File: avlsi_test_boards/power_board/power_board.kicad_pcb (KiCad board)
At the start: 6 copper layers, 99.9 x 100 mm, 100 parts, among them J1 PJ-102AH, J2 PJ-102AH, U1 TLV1117LV18DCYR, U11 TLV75709PDBV, U12 SN74LVC16T245DLR, U13 SN74LVC16T245DLR, U14 SN74LVC16T245DLR, U15 SN74LVC16T245DLR, U16 SN74LVC16T245DLR, U17 SN74LVC16T245DLR, U2 TLV1117LV25DCYR, U3 TLV1117LV33DCYR, U4 DS04-254-2-04BK-SMT, U5 74HC4051D_653, U6 TLV1117LV18DCYR, U7 TLV75709PDBV, U8 TLV1117LV25DCYR, U9 TLV1117LV33DCYR

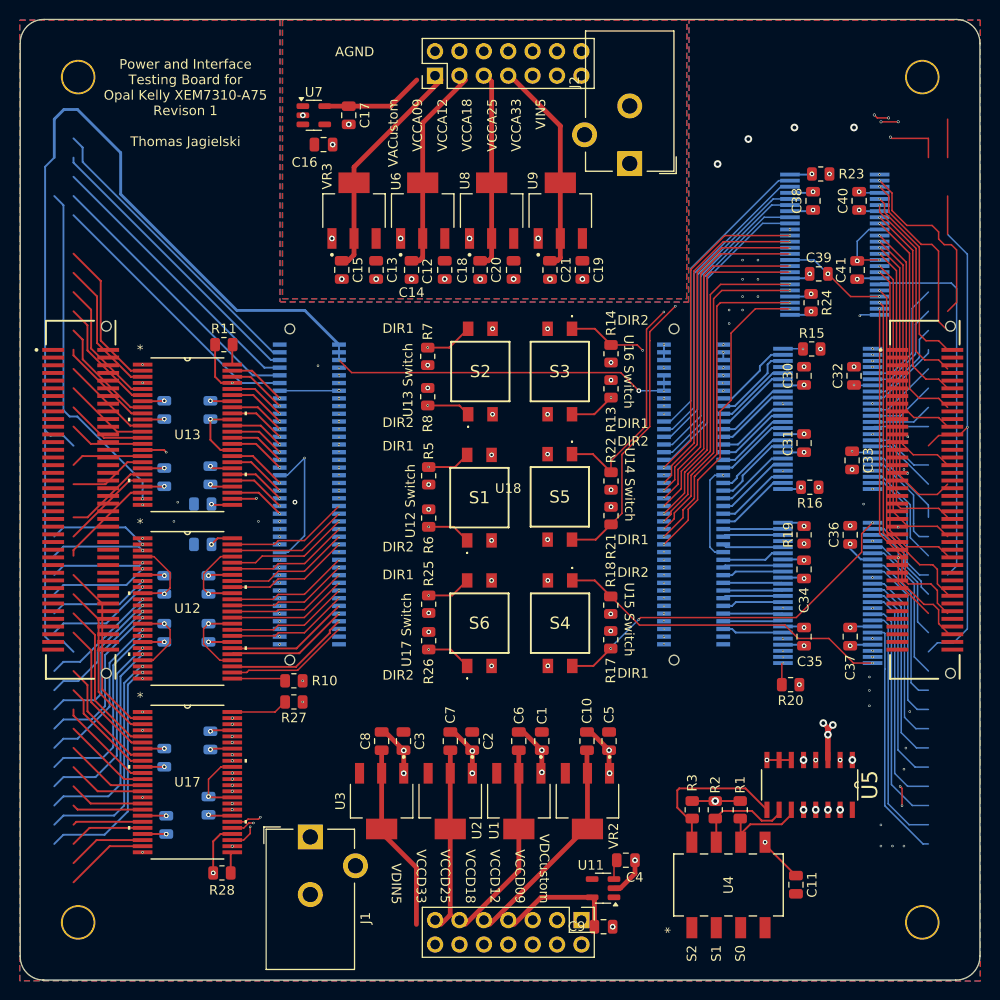
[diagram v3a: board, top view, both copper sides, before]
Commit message: Add updated power board layout and schematic
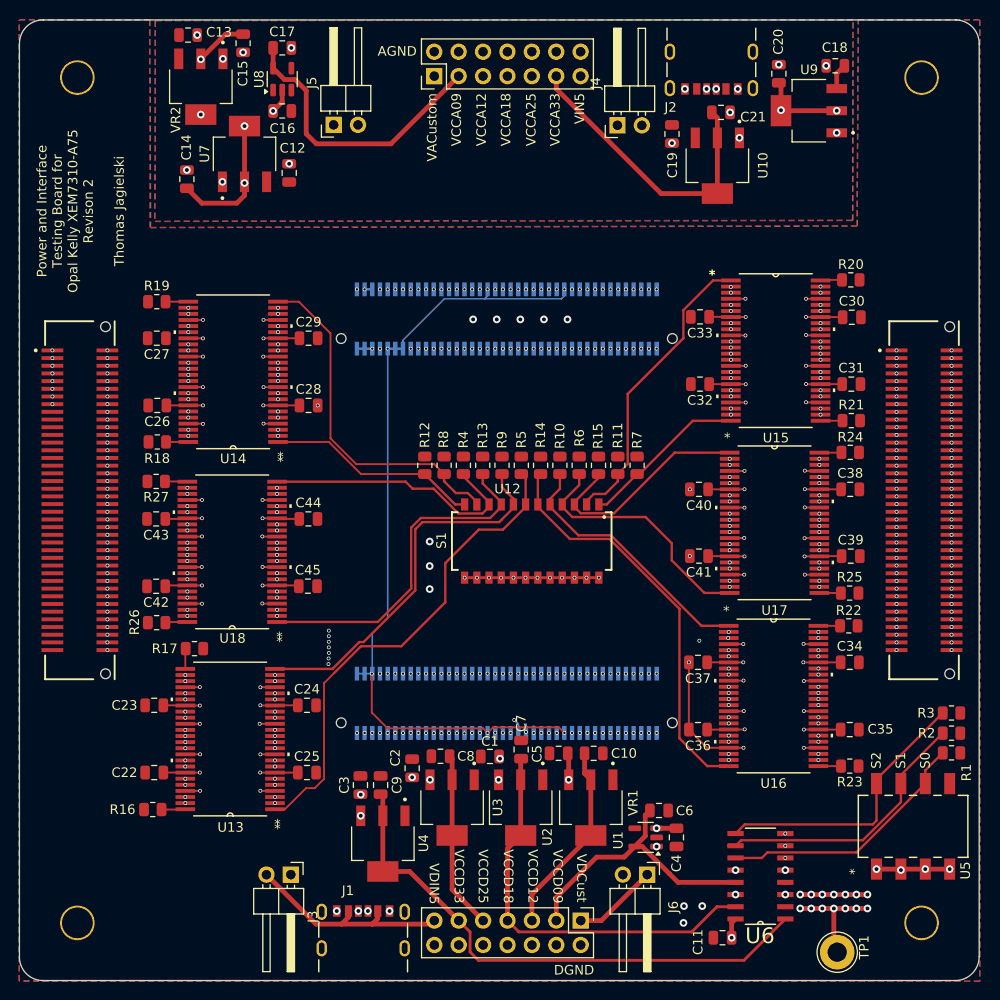
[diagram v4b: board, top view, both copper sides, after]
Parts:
- removed R28: 10k, Resistor_SMD:R_0805_2012Metric
- removed S2, S3, S4, S5, S6: 2454985-3, 2_DS:24549853
- removed VR3: TLV1117LV12DCYR, avlsi:VREG_TLV1117LV12DCYR
- added J3: Conn_01x02_Pin, Connector_PinHeader_2.54mm:PinHeader_1x02_P2.54mm_Horizontal, F.Cu at (128.4, 114.4)
- added J4: Conn_01x02_Pin, Connector_PinHeader_2.54mm:PinHeader_1x02_P2.54mm_Horizontal, F.Cu at (162.4, 36.4)
- added J5: Conn_01x02_Pin, Connector_PinHeader_2.54mm:PinHeader_1x02_P2.54mm_Horizontal, F.Cu at (132.8, 36.3)
- added J6: Conn_01x02_Pin, Connector_PinHeader_2.54mm:PinHeader_1x02_P2.54mm_Horizontal, F.Cu at (165.5, 114.4)
- added R4: 4.7k, Resistor_SMD:R_0805_2012Metric, F.Cu at (146.3, 71.8)
- added TP1: TestPoint, TestPoint:TestPoint_Loop_D3.80mm_Drill2.0mm, F.Cu at (185.2, 122.5)
- added VR1: TLV1117LV12DCYR, avlsi:VREG_TLV1117LV12DCYR, F.Cu at (159.6, 107.4)
- C22, C23, C24, C25, C26, C27, C28, C29, C42, C43, C44, C45, U14, U15, U16: moved to F.Cu
- J1, J2: value PJ-102AH -> 2171750001; footprint Connector_BarrelJack:BarrelJack_CUI_PJ-102AH_Horizontal -> avlsi_preferred_parts:MOLEX_2171750001
- R10, R11, R15: value 10k -> 4.7k
- R12, R9: value 10k -> 4.7k; moved to F.Cu
- R17, R18, R21, R22, R25, R26: value 4.7k -> 10k
- S1: value 2454985-3 -> 416131160812; footprint 2_DS:24549853 -> avlsi_preferred_parts:416131160812
- U1: value TLV1117LV18DCYR -> TLV75709PDBV; footprint avlsi:SOT230P700X180-4N -> Package_TO_SOT_SMD:SOT-23-5
- U10: value ~ -> TLV1117LV33DCYR; footprint avlsi:opal_kelly_XEM7310_header -> avlsi:VREG_TLV1117LV33DCYR; moved to F.Cu
- U11: value TLV75709PDBV -> ~; footprint Package_TO_SOT_SMD:SOT-23-5 -> avlsi:opal_kelly_XEM7310_header; moved to B.Cu
- U12: value SN74LVC16T245DLR -> ~; footprint avlsi:DL48 -> avlsi_preferred_parts:power_board
- U18: value ~ -> SN74LVC16T245DLR; footprint avlsi_preferred_parts:power_board -> avlsi:DL48
- U2: value TLV1117LV25DCYR -> TLV1117LV18DCYR
- U3, U9: value TLV1117LV33DCYR -> TLV1117LV25DCYR; footprint avlsi:VREG_TLV1117LV33DCYR -> avlsi:SOT230P700X180-4N
- U4: value DS04-254-2-04BK-SMT -> TLV1117LV33DCYR; footprint ds:DS04-254-2-04BK-SMT_CUD -> avlsi:VREG_TLV1117LV33DCYR
- U5: value 74HC4051D_653 -> DS04-254-2-04BK-SMT; footprint 74HC4051D_653:SOIC127P600X175-16N -> ds:DS04-254-2-04BK-SMT_CUD
- U6: value TLV1117LV18DCYR -> 74HC4051D_653; footprint avlsi:SOT230P700X180-4N -> 74HC4051D_653:SOIC127P600X175-16N
- U7: value TLV75709PDBV -> TLV1117LV18DCYR; footprint Package_TO_SOT_SMD:SOT-23-5 -> avlsi:SOT230P700X180-4N
- U8: value TLV1117LV25DCYR -> TLV75709PDBV; footprint avlsi:SOT230P700X180-4N -> Package_TO_SOT_SMD:SOT-23-5
- moved VR2 84.6 mm to (119.0, 32.4)
- moved U6 77.7 mm to (177.3, 114.5), turned to 180 degrees
- moved R16 76.2 mm to (114.0, 107.6), turned to 0 degrees
- moved R19 71.6 mm to (114.4, 54.7), turned to 0 degrees
- moved U17 66.8 mm to (178.7, 77.8)
- moved U14 62.1 mm to (122.4, 62.0)
- moved R23 61.7 mm to (186.6, 103.1)
- moved R18 50.2 mm to (114.5, 69.3), turned to 0 degrees
- moved U16 47.4 mm to (178.6, 95.8), turned to 0 degrees
- moved R25 43.8 mm to (186.5, 85.1), turned to 180 degrees
- moved R17 43.3 mm to (118.3, 90.8), turned to 180 degrees
- moved R11 42.9 mm to (162.4, 71.8), turned to -90 degrees
- moved R20 42.6 mm to (186.7, 52.5)
- moved U10 41.3 mm to (172.8, 40.6), turned to -90 degrees
- moved C25 40.6 mm to (130.1, 103.8), turned to 0 degrees
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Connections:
- C22 pad 1: VCCD33 -> V_Level_Shift
- C23 pad 1: VCCD33 -> V_Level_Shift
- C24 pad 1: V_Level_Shift -> VCCD33
- C25 pad 1: V_Level_Shift -> VCCD33
- C26 pad 1: VCCD33 -> V_Level_Shift
- C27 pad 1: VCCD33 -> V_Level_Shift
- C28 pad 1: V_Level_Shift -> VCCD33
- C29 pad 1: V_Level_Shift -> VCCD33
- C30 pad 1: VCCD33 -> V_Level_Shift
- C31 pad 1: VCCD33 -> V_Level_Shift
- C32 pad 1: V_Level_Shift -> VCCD33
- C33 pad 1: V_Level_Shift -> VCCD33
- C34 pad 1: VCCD33 -> V_Level_Shift
- C35 pad 1: VCCD33 -> V_Level_Shift
- C36 pad 1: V_Level_Shift -> VCCD33
- C37 pad 1: V_Level_Shift -> VCCD33
- C38 pad 1: VCCD33 -> V_Level_Shift
- C39 pad 1: VCCD33 -> V_Level_Shift
- C40 pad 1: V_Level_Shift -> VCCD33
- C41 pad 1: V_Level_Shift -> VCCD33
- C42 pad 1: VCCD33 -> V_Level_Shift
- C43 pad 1: VCCD33 -> V_Level_Shift
- C44 pad 1: V_Level_Shift -> VCCD33
- C45 pad 1: V_Level_Shift -> VCCD33
- C6 pad 1: VCCD18 -> VCCD09
- C7 pad 1: VCCD25 -> VCCD18
- C8 pad 1: VCCD33 -> VCCD25
- C9 pad 1: VCCD09 -> VCCD33
- R10 pad 2: Net-(U12-*2OE) -> /level_shifters/LS10_DIR1
- R11 pad 2: Net-(U13-*1OE) -> /level_shifters/LS9_DIR1
- R12 pad 2: Net-(U13-*2OE) -> /level_shifters/LS8_DIR1
- R13 pad 1: /level_shifter3/DIR1 -> DGND
- R13 pad 2: DGND -> /level_shifters/LS12_DIR1
- R14 pad 1: /level_shifter3/DIR2 -> DGND
- R14 pad 2: DGND -> /level_shifters/LS10_DIR2
- R15 pad 2: Net-(U14-*1OE) -> /level_shifters/LS11_DIR1
- R16 pad 2: Net-(U14-*2OE) -> Net-(U13-*1OE)
- R17 pad 1: /level_shifter4/DIR1 -> DGND
- R17 pad 2: DGND -> Net-(U13-*2OE)
- R18 pad 1: /level_shifter4/DIR2 -> DGND
- R18 pad 2: DGND -> Net-(U14-*1OE)
- R19 pad 2: Net-(U15-*1OE) -> Net-(U14-*2OE)
- R20 pad 2: Net-(U15-*2OE) -> Net-(U15-*1OE)
- R21 pad 1: /level_shifter5/DIR1 -> DGND
- R21 pad 2: DGND -> Net-(U15-*2OE)
- R22 pad 1: /level_shifter5/DIR2 -> DGND
- R22 pad 2: DGND -> Net-(U16-*1OE)
- R23 pad 2: Net-(U16-*1OE) -> Net-(U16-*2OE)
- R24 pad 2: Net-(U16-*2OE) -> Net-(U17-*1OE)
- R25 pad 1: /level_shifter6/DIR1 -> DGND
- R25 pad 2: DGND -> Net-(U17-*2OE)
- R26 pad 1: /level_shifter6/DIR2 -> DGND
- R26 pad 2: DGND -> Net-(U18-*1OE)
- R27 pad 2: Net-(U17-*1OE) -> Net-(U18-*2OE)
- R5 pad 1: /level_shifter1/DIR1 -> DGND
- R5 pad 2: DGND -> /level_shifters/LS7_DIR1
- R6 pad 1: /level_shifter1/DIR2 -> DGND
- R6 pad 2: DGND -> /level_shifters/LS11_DIR2
- R7 pad 1: /level_shifter2/DIR1 -> DGND
- R7 pad 2: DGND -> /level_shifters/LS9_DIR2
- R8 pad 1: /level_shifter2/DIR2 -> DGND
- R8 pad 2: DGND -> /level_shifters/LS8_DIR2
- R9 pad 2: Net-(U12-*1OE) -> /level_shifters/LS7_DIR2
- S1 pad A1: /level_shifter1/DIR2 -> VCCD33
- U1 pad 1: DGND -> DVIN5
- U1 pad 2: VCCD18 -> DGND
- U1 pad 4: VCCD18 -> unconnected-(U1-NC-Pad4)
- U12 pad 10: DGND -> MC1_19_PIN
- U12 pad 11: MC2_58_PIN -> MC1_26_PIN
- U12 pad 12: MC2_60_PIN -> MC1_21_PIN
- U12 pad 13: MC2_62_PIN -> MC1_28_PIN
- U12 pad 14: MC2_64_PIN -> MC1_23_PIN
- U12 pad 15: DGND -> MC1_30_PIN
- U12 pad 16: MC2_66_PIN -> MC1_25_PIN
- U12 pad 17: MC2_68_PIN -> unconnected-(U12A-MC1_17-Pad17)
- U12 pad 18: V_Level_Shift -> MC1_27_PIN
- U12 pad 19: MC2_70_PIN -> unconnected-(U12A-MC1_19-Pad19)
- U12 pad 20: MC2_72_PIN -> MC1_29_PIN
- U12 pad 21: DGND -> unconnected-(U12A-MC1_21-Pad21)
- U12 pad 22: MC2_74_PIN -> MC1_31_PIN
- U12 pad 23: MC2_76_PIN -> unconnected-(U12A-MC1_23-Pad23)
- U12 pad 24: /level_shifter1/DIR2 -> MC1_33_PIN
- U12 pad 25: Net-(U12-*2OE) -> unconnected-(U12A-MC1_25-Pad25)
- U12 pad 26: MC2_76 -> MC1_37_PIN
- U12 pad 27: MC2_74 -> unconnected-(U12A-MC1_27-Pad27)
- U12 pad 28: DGND -> MC1_39_PIN
- U12 pad 29: MC2_72 -> unconnected-(U12A-MC1_29-Pad29)
- U12 pad 30: MC2_70 -> MC1_41_PIN
- U12 pad 31: VCCD33 -> unconnected-(U12A-MC1_31-Pad31)
- U12 pad 32: MC2_68 -> MC1_43_PIN
- U12 pad 33: MC2_66 -> unconnected-(U12A-MC1_33-Pad33)
- U12 pad 34: DGND -> MC2_26_PIN
- U12 pad 35: MC2_64 -> unconnected-(U12A-DGND-Pad35)
- U12 pad 36: MC2_62 -> MC2_24_PIN
- U12 pad 37: MC2_60 -> unconnected-(U12A-MC1_37-Pad37)
- U12 pad 38: MC2_58 -> MC2_22_PIN
- U12 pad 39: DGND -> unconnected-(U12A-MC1_39-Pad39)
- U12 pad 40: MC2_54 -> MC2_20_PIN
- U12 pad 41: MC2_52 -> unconnected-(U12A-MC1_41-Pad41)
- U12 pad 42: VCCD33 -> MC2_18_PIN
- U12 pad 43: MC2_50 -> unconnected-(U12A-MC1_43-Pad43)
- U12 pad 44: MC2_48 -> MC2_16_PIN
- U12 pad 45: DGND -> unconnected-(U12A-MC1_45-Pad45)
- U12 pad 46: MC2_46 -> MC2_12_PIN
- U12 pad 47: MC2_44 -> unconnected-(U12A-MC1_47-Pad47)
- U12 pad 48: Net-(U12-*1OE) -> MC2_10_PIN
- U13 pad 1: /level_shifter2/DIR1 -> /level_shifters/LS7_DIR1
- U13 pad 11: MC2_27_PIN -> MC2_17
- U13 pad 12: MC2_29_PIN -> MC2_15
- U13 pad 13: MC2_31_PIN -> MC2_31
- U13 pad 14: MC2_33_PIN -> MC2_33
- U13 pad 16: MC2_37_PIN -> MC2_37
- U13 pad 17: MC2_39_PIN -> MC2_39
- U13 pad 18: V_Level_Shift -> VCCD33
- U13 pad 19: MC2_41_PIN -> MC2_41
- U13 pad 2: MC2_15_PIN -> MC2_29
- U13 pad 20: MC2_43_PIN -> MC2_43
- U13 pad 22: MC2_45_PIN -> MC2_45
- U13 pad 23: MC2_10_PIN -> MC2_47
- U13 pad 24: /level_shifter2/DIR2 -> /level_shifters/LS7_DIR2
- U13 pad 26: MC2_10 -> MC2_47_PIN
- U13 pad 27: MC2_45 -> MC2_45_PIN
- U13 pad 29: MC2_43 -> MC2_43_PIN
- U13 pad 3: MC2_17_PIN -> MC2_27
- U13 pad 30: MC2_41 -> MC2_41_PIN
- U13 pad 31: VCCD33 -> V_Level_Shift
- U13 pad 32: MC2_39 -> MC2_39_PIN
- U13 pad 33: MC2_37 -> MC2_37_PIN
- U13 pad 35: MC2_33 -> MC2_33_PIN
- U13 pad 36: MC2_31 -> MC2_31_PIN
- U13 pad 37: MC2_29 -> MC2_15_PIN
- U13 pad 38: MC2_27 -> MC2_17_PIN
- U13 pad 40: MC2_25 -> MC2_19_PIN
- U13 pad 41: MC2_23 -> MC2_21_PIN
- U13 pad 42: VCCD33 -> V_Level_Shift
- U13 pad 43: MC2_21 -> MC2_23_PIN
- U13 pad 44: MC2_19 -> MC2_25_PIN
- U13 pad 46: MC2_17 -> MC2_27_PIN
- U13 pad 47: MC2_15 -> MC2_29_PIN
- U13 pad 5: MC2_19_PIN -> MC2_25
- U13 pad 6: MC2_21_PIN -> MC2_23
- U13 pad 7: V_Level_Shift -> VCCD33
- U13 pad 8: MC2_23_PIN -> MC2_21
- U13 pad 9: MC2_25_PIN -> MC2_19
- U14 pad 1: /level_shifter3/DIR1 -> /level_shifters/LS8_DIR1
- U14 pad 11: MC1_28_PIN -> MC1_34
- U14 pad 12: MC1_30_PIN -> MC1_32
- U14 pad 13: MC1_32_PIN -> MC1_30
- U14 pad 14: MC1_34_PIN -> MC1_28
- U14 pad 16: MC1_38_PIN -> MC1_26
- U14 pad 17: MC1_40_PIN -> MC1_24
- U14 pad 18: V_Level_Shift -> VCCD33
- U14 pad 19: MC1_42_PIN -> MC1_22
- U14 pad 2: MC1_16_PIN -> MC1_25
- U14 pad 20: MC1_44_PIN -> MC1_20
- U14 pad 22: MC1_46_PIN -> MC1_18
- U14 pad 23: MC1_48_PIN -> MC1_16
- U14 pad 24: /level_shifter3/DIR2 -> /level_shifters/LS8_DIR2
- U14 pad 26: MC1_48 -> MC1_16_PIN
- U14 pad 27: MC1_46 -> MC1_18_PIN
- U14 pad 29: MC1_44 -> MC1_20_PIN
- U14 pad 3: MC1_18_PIN -> MC1_23
- U14 pad 30: MC1_42 -> MC1_22_PIN
- U14 pad 31: VCCD33 -> V_Level_Shift
- U14 pad 32: MC1_40 -> MC1_24_PIN
- U14 pad 33: MC1_38 -> MC1_26_PIN
- U14 pad 35: MC1_34 -> MC1_28_PIN
- U14 pad 36: MC1_32 -> MC1_30_PIN
- U14 pad 37: MC1_30 -> MC1_32_PIN
- U14 pad 38: MC1_28 -> MC1_34_PIN
- U14 pad 40: MC1_26 -> MC1_15_PIN
- U14 pad 41: MC1_24 -> MC1_17_PIN
- U14 pad 42: VCCD33 -> V_Level_Shift
- U14 pad 43: MC1_22 -> MC1_19_PIN
- U14 pad 44: MC1_20 -> MC1_21_PIN
- U14 pad 46: MC1_18 -> MC1_23_PIN
- U14 pad 47: MC1_16 -> MC1_25_PIN
- U14 pad 5: MC1_20_PIN -> MC1_21
- U14 pad 6: MC1_22_PIN -> MC1_19
- U14 pad 7: V_Level_Shift -> VCCD33
- U14 pad 8: MC1_24_PIN -> MC1_17
- U14 pad 9: MC1_26_PIN -> MC1_15
- U15 pad 1: /level_shifter4/DIR1 -> /level_shifters/LS9_DIR1
- U15 pad 11: MC1_64_PIN -> MC1_64
- U15 pad 12: MC1_66_PIN -> MC1_62
- U15 pad 13: MC1_68_PIN -> MC1_60
- U15 pad 14: MC1_70_PIN -> MC1_58
- U15 pad 16: MC1_72_PIN -> MC1_54
- U15 pad 17: MC1_74_PIN -> MC1_52
- U15 pad 18: V_Level_Shift -> VCCD33
- U15 pad 19: MC1_76_PIN -> MC1_50
- U15 pad 2: MC1_50_PIN -> MC1_74
- U15 pad 20: MC1_15_PIN -> MC1_79
- U15 pad 22: MC1_17_PIN -> MC1_77
- U15 pad 23: MC1_19_PIN -> MC1_75
- U15 pad 24: /level_shifter4/DIR2 -> /level_shifters/LS9_DIR2
- U15 pad 26: MC1_19 -> MC1_75_PIN
- U15 pad 27: MC1_17 -> MC1_77_PIN
- U15 pad 29: MC1_15 -> MC1_79_PIN
- U15 pad 3: MC1_52_PIN -> MC1_76
- U15 pad 30: MC1_76 -> MC1_50_PIN
- U15 pad 31: VCCD33 -> V_Level_Shift
- U15 pad 32: MC1_74 -> MC1_52_PIN
- U15 pad 33: MC1_72 -> MC1_54_PIN
- U15 pad 35: MC1_70 -> MC1_58_PIN
- U15 pad 36: MC1_68 -> MC1_60_PIN
- U15 pad 37: MC1_66 -> MC1_62_PIN
- U15 pad 38: MC1_64 -> MC1_64_PIN
- U15 pad 40: MC1_62 -> MC1_66_PIN
- U15 pad 41: MC1_60 -> MC1_68_PIN
- U15 pad 42: VCCD33 -> V_Level_Shift
- U15 pad 43: MC1_58 -> MC1_70_PIN
- U15 pad 44: MC1_54 -> MC1_72_PIN
- U15 pad 46: MC1_52 -> MC1_76_PIN
- U15 pad 47: MC1_50 -> MC1_74_PIN
- U15 pad 5: MC1_54_PIN -> MC1_72
- U15 pad 6: MC1_58_PIN -> MC1_70
- U15 pad 7: V_Level_Shift -> VCCD33
- U15 pad 8: MC1_60_PIN -> MC1_68
- U15 pad 9: MC1_62_PIN -> MC1_66
- U16 pad 1: /level_shifter5/DIR1 -> /level_shifters/LS10_DIR1
- U16 pad 11: MC1_33_PIN -> MC2_73
- U16 pad 12: MC1_37_PIN -> MC2_75
- U16 pad 13: MC1_39_PIN -> MC2_77
- U16 pad 14: MC1_41_PIN -> MC2_79
- U16 pad 16: MC1_43_PIN -> MC2_61
- U16 pad 17: MC1_45_PIN -> MC2_59
- U16 pad 18: V_Level_Shift -> VCCD33
- U16 pad 19: MC1_47_PIN -> MC2_57
- U16 pad 2: MC1_21_PIN -> MC2_76
- U16 pad 20: MC1_49_PIN -> MC2_53
- U16 pad 22: MC1_51_PIN -> MC2_51
- U16 pad 23: MC1_53_PIN -> MC2_49
- U16 pad 24: /level_shifter5/DIR2 -> /level_shifters/LS10_DIR2
- U16 pad 26: MC1_53 -> MC2_49_PIN
- U16 pad 27: MC1_51 -> MC2_51_PIN
- U16 pad 29: MC1_49 -> MC2_53_PIN
- U16 pad 3: MC1_23_PIN -> MC2_63
- U16 pad 30: MC1_47 -> MC2_57_PIN
- U16 pad 31: VCCD33 -> V_Level_Shift
- U16 pad 32: MC1_45 -> MC2_59_PIN
- U16 pad 33: MC1_43 -> MC2_61_PIN
- U16 pad 35: MC1_41 -> MC2_79_PIN
- U16 pad 36: MC1_39 -> MC2_77_PIN
- U16 pad 37: MC1_37 -> MC2_75_PIN
- U16 pad 38: MC1_33 -> MC2_73_PIN
- U16 pad 40: MC1_31 -> MC2_71_PIN
- U16 pad 41: MC1_29 -> MC2_69_PIN
- U16 pad 42: VCCD33 -> V_Level_Shift
- U16 pad 43: MC1_27 -> MC2_67_PIN
- U16 pad 44: MC1_25 -> MC2_65_PIN
- U16 pad 46: MC1_23 -> MC2_63_PIN
- U16 pad 47: MC1_21 -> MC2_76_PIN
- U16 pad 5: MC1_25_PIN -> MC2_65
- U16 pad 6: MC1_27_PIN -> MC2_67
- U16 pad 7: V_Level_Shift -> VCCD33
- U16 pad 8: MC1_29_PIN -> MC2_69
- U16 pad 9: MC1_31_PIN -> MC2_71
- U17 pad 1: /level_shifter6/DIR1 -> /level_shifters/LS11_DIR1
- U17 pad 11: MC2_61_PIN -> MC1_61
- U17 pad 12: MC2_63_PIN -> MC1_59
- U17 pad 13: MC2_65_PIN -> MC2_60
- U17 pad 14: MC2_67_PIN -> MC2_62
- U17 pad 16: MC2_69_PIN -> MC2_64
- U17 pad 17: MC2_71_PIN -> MC2_66
- U17 pad 18: V_Level_Shift -> VCCD33
- U17 pad 19: MC2_73_PIN -> MC2_68
- U17 pad 2: MC2_47_PIN -> MC1_73
- U17 pad 20: MC2_75_PIN -> MC2_70
- U17 pad 22: MC2_77_PIN -> MC2_72
- U17 pad 23: MC2_79_PIN -> MC2_74
- U17 pad 24: /level_shifter6/DIR2 -> /level_shifters/LS11_DIR2
- U17 pad 26: MC2_79 -> MC2_74_PIN
- U17 pad 27: MC2_77 -> MC2_72_PIN
- U17 pad 29: MC2_75 -> MC2_70_PIN
- U17 pad 3: MC2_49_PIN -> MC1_71
- U17 pad 30: MC2_73 -> MC2_68_PIN
- U17 pad 31: VCCD33 -> V_Level_Shift
- U17 pad 32: MC2_71 -> MC2_66_PIN
- U17 pad 33: MC2_69 -> MC2_64_PIN
- U17 pad 35: MC2_67 -> MC2_62_PIN
- U17 pad 36: MC2_65 -> MC2_60_PIN
- U17 pad 37: MC2_63 -> MC1_59_PIN
- U17 pad 38: MC2_61 -> MC1_61_PIN
- U17 pad 40: MC2_59 -> MC1_63_PIN
- U17 pad 41: MC2_57 -> MC1_65_PIN
- U17 pad 42: VCCD33 -> V_Level_Shift
- U17 pad 43: MC2_53 -> MC1_67_PIN
- U17 pad 44: MC2_51 -> MC1_69_PIN
- U17 pad 46: MC2_49 -> MC1_71_PIN
- U17 pad 47: MC2_47 -> MC1_73_PIN
- U17 pad 5: MC2_51_PIN -> MC1_69
- U17 pad 6: MC2_53_PIN -> MC1_67
- U17 pad 7: V_Level_Shift -> VCCD33
- U17 pad 8: MC2_57_PIN -> MC1_65
- U17 pad 9: MC2_59_PIN -> MC1_63
- U18 pad 10: FPGA_TDI -> DGND
- U18 pad 11: MC2_12 -> MC2_24
- U18 pad 12: SYS_CLK_MC2 -> MC2_26
- U18 pad 13: DGND -> MC1_43
- U18 pad 14: DGND -> MC1_41
- U18 pad 15: MC2_16 -> DGND
- U18 pad 16: MC2_15_PIN -> MC1_39
- U18 pad 17: MC2_18 -> MC1_37
- U18 pad 18: MC2_17_PIN -> VCCD33
- U18 pad 19: MC2_20 -> MC1_33
- U18 pad 20: MC2_19_PIN -> MC1_31
- U18 pad 21: MC2_22 -> DGND
- U18 pad 22: MC2_21_PIN -> MC1_29
- U18 pad 23: MC2_24 -> MC1_27
- U18 pad 24: MC2_23_PIN -> /level_shifters/LS12_DIR2
- U18 pad 25: MC2_26 -> Net-(U18-*2OE)
- U18 pad 26: MC2_25_PIN -> MC1_27_PIN
- U18 pad 27: MC2_28 -> MC1_29_PIN
- U18 pad 28: MC2_27_PIN -> DGND
- U18 pad 29: MC2_30 -> MC1_31_PIN
- U18 pad 30: MC2_29_PIN -> MC1_33_PIN
- U18 pad 31: MC2_32 -> V_Level_Shift
- U18 pad 32: MC2_31_PIN -> MC1_37_PIN
- U18 pad 33: MC2_34 -> MC1_39_PIN
- U18 pad 34: MC2_33_PIN -> DGND
- U18 pad 35: DGND -> MC1_41_PIN
- U18 pad 36: FPGA_33VDD -> MC1_43_PIN
- U18 pad 37: MC2_38 -> MC2_26_PIN
- U18 pad 38: MC2_37_PIN -> MC2_24_PIN
- U18 pad 39: MC2_40 -> DGND
- U18 pad 40: MC2_39_PIN -> MC2_22_PIN
- U18 pad 41: MC2_42 -> MC2_20_PIN
- U18 pad 42: MC2_41_PIN -> V_Level_Shift
- U18 pad 43: MC2_44_PIN -> MC2_18_PIN
- U18 pad 44: MC2_43_PIN -> MC2_16_PIN
- U18 pad 45: MC2_46_PIN -> DGND
- U18 pad 46: MC2_45_PIN -> MC2_12_PIN
- U18 pad 47: MC2_48_PIN -> MC2_10_PIN
- U18 pad 48: MC2_47_PIN -> Net-(U18-*1OE)
- U2 pad 2: VCCD25 -> VCCD18
- U2 pad 4: VCCD25 -> VCCD18
- U3 pad 2: VCCD33 -> VCCD25
- U3 pad 4: VCCD33 -> VCCD25
- U4 pad 1: DVIN5 -> DGND
- U4 pad 2: DVIN5 -> VCCD33
- U4 pad 4: DVIN5 -> VCCD33
- U5 pad 1: VCCD33 -> DVIN5
- U5 pad 2: DGND -> DVIN5
- U5 pad 3: V_Level_Shift -> DVIN5
- U5 pad 4: DGND -> DVIN5
- U5 pad 5: VDCustom -> DGND
- U5 pad 6: DGND -> /digital_power_converters/S0
- U5 pad 7: DGND -> /digital_power_converters/S1
- U5 pad 8: DGND -> /digital_power_converters/S2
- U6 pad 1: AGND -> VCCD33
- U6 pad 2: VCCA18 -> DGND
- U6 pad 3: AVIN5 -> V_Level_Shift
- U6 pad 4: VCCA18 -> DGND
- U7 pad 1: AVIN5 -> AGND
- U7 pad 2: AGND -> VCCA18
- U7 pad 4: unconnected-(U7-NC-Pad4) -> VCCA18
- U8 pad 1: AGND -> AVIN5
- U8 pad 2: VCCA25 -> AGND
- U8 pad 4: VCCA25 -> unconnected-(U8-NC-Pad4)
- U9 pad 2: VCCA33 -> VCCA25
- U9 pad 4: VCCA33 -> VCCA25
- VR2 pad 1: DGND -> AGND
- VR2 pad 2: VCCD12 -> VCCA12
- VR2 pad 3: DVIN5 -> AVIN5
- VR2 pad 4: VCCD12 -> VCCA12
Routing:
- net DVIN5: track 2.08 -> 168.2 mm, vias 0 -> 14
- net FPGA_33VDD: track 220.9 -> 84.5 mm
- net DGND: track 156.5 -> 85.4 mm, vias 121 -> 84
- net MC1_23_PIN: track 70.4 -> 9.86 mm
- net XADC_VP: track 60.0 -> 0.00 mm
- net FPGA_18VDD: track 57.8 -> 0.00 mm
- net XADC_VN: track 57.6 -> 0.00 mm, vias 3 -> 1
- net /level_shifter5/DIR1: track 57.1 -> 0.00 mm, vias 2 -> 0
- net FPGA_VCDIN: track 57.4 -> 1.60 mm
- net SYS_CLK_MC1: track 54.2 -> 0.00 mm, vias 3 -> 1
- net V_Level_Shift: track 36.1 -> 88.1 mm, vias 15 -> 27
- net /level_shifters/LS7_DIR1: track 0.00 -> 51.0 mm
- net /level_shifter1/DIR2: track 47.4 -> 0.00 mm, vias 2 -> 0
- net /level_shifter5/DIR2: track 47.1 -> 0.00 mm, vias 2 -> 0
- net FPGA_TDO: track 46.7 -> 0.00 mm
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- added copper zone on F.Cu, net DGND
- added copper zone on In2.Cu, net VCCD33
- added copper zone on In1.Cu, net V_Level_Shift
- removed copper zone on In3.Cu, net DGND
- removed copper zone on In4.Cu, net DGND
- removed copper zone on F.Cu, net DVIN5
- removed copper zone on In1.Cu, net VCCD33
- removed copper zone on In2.Cu, net V_Level_Shift
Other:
- copper layers 6 -> 4
- board text added: "AVIN5"
- board text added: "DGND"
- board text added: "DVIN"
- board text added: "Power and Interface Testing Board for Opal Kelly XEM7310-A75 Revison 2 Thomas Jagielski"
- board text added: "VCCACUSTOM"
- board text added: "VDCUSTOM"
- board text added: "VDCust"
- board text removed: "DIR1"
- board text removed: "DIR2"
- board text removed: "Power and Interface Testing Board for Opal Kelly XEM7310-A75 Revison 1 Thomas Jagielski"
- board text removed: "U12 Switch"
- board text removed: "U13 Switch"
- board text removed: "U14 Switch"
- board text removed: "U15 Switch"
- board text removed: "U16 Switch"
- board text removed: "U17 Switch"
- board text removed: "VDCustom"
